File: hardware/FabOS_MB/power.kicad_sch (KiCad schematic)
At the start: 22 parts, among them U501 TDPOWER TAS12-5-W2, U502 TPS563201

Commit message: create pcb
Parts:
- JP501: footprint Jumper:SolderJumper-2_P1.3mm_Open_Pad1.0x1.5mm -> Jumper:SolderJumper-2_P1.3mm_Open_TrianglePad1.0x1.5mm
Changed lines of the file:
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@@
 			)
 		)
-		(property "Footprint" "Jumper:SolderJumper-2_P1.3mm_Open_Pad1.0x1.5mm"
+		(property "Footprint" "Jumper:SolderJumper-2_P1.3mm_Open_TrianglePad1.0x1.5mm"
 			(at 82.55 36.83 0)
 			(effects

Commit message: Placement des composants
On va mourir
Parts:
- C502, C503: footprint Capacitor_SMD:C_Elec_4x5.4 -> Capacitor_SMD:C_0402_1005Metric; LCSC C213487 -> C15525; MPN VT1C100M0405 -> CL05A106MQ5NUNC
- C505: footprint Capacitor_SMD:C_Elec_6.3x5.4 -> Capacitor_SMD:C_0201_0603Metric_Pad0.64x0.40mm_HandSolder; LCSC C72505 -> C59461; MPN RVT1H220M0605 -> CL10A226MQ8NRNC
- C506: footprint Capacitor_SMD:C_Elec_6.3x5.4 -> Capacitor_SMD:C_0201_0603Metric_Pad0.64x0.40mm_HandSolder; LCSC (none) -> C59461; MPN (none) -> CL10A226MQ8NRNC
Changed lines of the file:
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@@
 			)
 		)
-		(property "Footprint" "Capacitor_SMD:C_Elec_6.3x5.4"
+		(property "Footprint" "Capacitor_SMD:C_0201_0603Metric_Pad0.64x0.40mm_HandSolder"
 			(at 210.82 116.84 0)
 			(effects
@@
 			)
 		)
-		(property "Datasheet" "https://www.lcsc.com/product-detail/Aluminum-Electrolytic-Capacitors-SMD_ROQANG-RVT1H220M0605_C72505.html"
+		(property "Datasheet" "https://www.lcsc.com/datasheet/lcsc_datasheet_2304140030_Samsung-Electro-Mechanics-CL10A226MQ8NRNC_C59461.pdf"
 			(at 210.82 116.84 0)
 			(effects
@@
 			)
 		)
-		(property "MPN" " RVT1H220M0605"
+		(property "MPN" "CL10A226MQ8NRNC"
 			(at 210.82 116.84 0)
 			(effects
@@
 			)
 		)
-		(property "LCSC" " C72505"
+		(property "LCSC" "C59461"
 			(at 210.82 116.84 0)
 			(effects
@@
 				(path "/09377d5d-727f-4ff4-92c8-7a0483d23f1e/97fc260e-c16c-48c4-b11a-4f8ec3a451f5"
 					(reference "C505")
+					(unit 1)
+				)
+			)
+		)
+	)
+	(symbol
+		(lib_id "Device:C_Small")
+		(at 220.98 116.84 0)
+		(mirror y)
+		(unit 1)
+		(exclude_from_sim no)
+		(in_bom yes)
+		(on_board yes)
+		(dnp no)
+		(fields_autoplaced yes)
+		(property "Reference" "C506"
+			(at 218.44 115.5762 0)
+			(effects
+				(font
+					(size 1.27 1.27)
+				)
+				(justify left)
+			)
+		)
+		(property "Value" "22u"
+			(at 218.44 118.1162 0)
+			(effects
+				(font
+					(size 1.27 1.27)
+				)
+				(justify left)
+			)
+		)
+		(property "Footprint" "Capacitor_SMD:C_0201_0603Metric_Pad0.64x0.40mm_HandSolder"
+			(at 220.98 116.84 0)
+			(effects
+				(font
+					(size 1.27 1.27)
+				)
+				(hide yes)
+			)
+		)
+		(property "Datasheet" "https://www.lcsc.com/datasheet/lcsc_datasheet_2304140030_Samsung-Electro-Mechanics-CL10A226MQ8NRNC_C59461.pdf"
+			(at 220.98 116.84 0)
+			(effects
+				(font
+					(size 1.27 1.27)
+				)
+				(hide yes)
+			)
+		)
+		(property "Description" "Unpolarized capacitor, small symbol"
+			(at 220.98 116.84 0)
+			(effects
+				(font
+					(size 1.27 1.27)
+				)
+				(hide yes)
+			)
+		)
+		(property "MPN" "CL10A226MQ8NRNC"
+			(at 220.98 116.84 0)
+			(effects
+				(font
+					(size 1.27 1.27)
+				)
+				(hide yes)
+			)
+		)
+		(property "LCSC" "C59461"
+			(at 220.98 116.84 0)
+			(effects
+				(font
+					(size 1.27 1.27)
+				)
+				(hide yes)
+			)
+		)
+		(pin "1"
+		)
+		(pin "2"
+		)
+		(instances
+			(project "FabOS_MB"
+				(path "/09377d5d-727f-4ff4-92c8-7a0483d23f1e/97fc260e-c16c-48c4-b11a-4f8ec3a451f5"
+					(reference "C506")
 					(unit 1)
 				)
@@
 	(symbol
 		(lib_id "Device:C_Small")
-		(at 220.98 116.84 0)
-		(mirror y)
-		(unit 1)
-		(exclude_from_sim no)
-		(in_bom yes)
-		(on_board yes)
-		(dnp no)
-		(fields_autoplaced yes)
-		(property "Reference" "C506"
-			(at 218.44 115.5762 0)
-			(effects
-				(font
-					(size 1.27 1.27)
-				)
-				(justify left)
-			)
-		)
-		(property "Value" "22u"
-			(at 218.44 118.1162 0)
-			(effects
-				(font
-					(size 1.27 1.27)
-				)
-				(justify left)
-			)
-		)
-		(property "Footprint" "Capacitor_SMD:C_Elec_6.3x5.4"
-			(at 220.98 116.84 0)
-			(effects
-				(font
-					(size 1.27 1.27)
-				)
-				(hide yes)
-			)
-		)
-		(property "Datasheet" "~"
-			(at 220.98 116.84 0)
-			(effects
-				(font
-					(size 1.27 1.27)
-				)
-				(hide yes)
-			)
-		)
-		(property "Description" "Unpolarized capacitor, small symbol"
-			(at 220.98 116.84 0)
-			(effects
-				(font
-					(size 1.27 1.27)
-				)
-				(hide yes)
-			)
-		)
-		(pin "1"
-		)
-		(pin "2"
-		)
-		(instances
-			(project "FabOS_MB"
-				(path "/09377d5d-727f-4ff4-92c8-7a0483d23f1e/97fc260e-c16c-48c4-b11a-4f8ec3a451f5"
-					(reference "C506")
-					(unit 1)
-				)
-			)
-		)
-	)
-	(symbol
-		(lib_id "Device:C_Small")
 		(at 184.15 109.22 0)
 		(unit 1)
@@
 			)
 		)
-		(property "Footprint" "Capacitor_SMD:C_Elec_4x5.4"
+		(property "Footprint" "Capacitor_SMD:C_0402_1005Metric"
 			(at 129.54 109.22 0)
 			(effects
@@
 			)
 		)
-		(property "Datasheet" "https://www.lcsc.com/product-detail/Aluminum-Electrolytic-Capacitors-SMD_ROQANG-VT1C100M0405_C213487.html"
+		(property "Datasheet" "https://www.lcsc.com/datasheet/lcsc_datasheet_2208231630_Samsung-Electro-Mechanics-CL05A106MQ5NUNC_C15525.pdf"
 			(at 129.54 109.22 0)
 			(effects
@@
 			)
 		)
-		(property "MPN" "VT1C100M0405"
+		(property "MPN" "CL05A106MQ5NUNC"
 			(at 131.572 116.332 0)
 			(effects
@@
 			)
 		)
-		(property "LCSC" " C213487"
+		(property "LCSC" "C15525"
 			(at 129.54 109.22 0)
 			(effects
@@
 	)
 	(symbol
+		(lib_id "Device:C_Small")
+		(at 138.43 109.22 0)
+		(unit 1)
+		(exclude_from_sim no)
+		(in_bom yes)
+		(on_board yes)
+		(dnp no)
+		(property "Reference" "C503"
+			(at 132.08 110.744 0)
+			(effects
+				(font
+					(size 1.27 1.27)
+				)
+				(justify left)
+			)
+		)
+		(property "Value" "10u"
+			(at 133.35 107.95 0)
+			(effects
+				(font
+					(size 1.27 1.27)
+				)
+				(justify left)
+			)
+		)
+		(property "Footprint" "Capacitor_SMD:C_0402_1005Metric"
+			(at 138.43 109.22 0)
+			(effects
+				(font
+					(size 1.27 1.27)
+				)
+				(hide yes)
+			)
+		)
+		(property "Datasheet" "https://www.lcsc.com/datasheet/lcsc_datasheet_2208231630_Samsung-Electro-Mechanics-CL05A106MQ5NUNC_C15525.pdf"
+			(at 138.43 109.22 0)
+			(effects
+				(font
+					(size 1.27 1.27)
+				)
+				(hide yes)
+			)
+		)
+		(property "Description" "Unpolarized capacitor, small symbol"
+			(at 138.43 109.22 0)
+			(effects
+				(font
+					(size 1.27 1.27)
+				)
+				(hide yes)
+			)
+		)
+		(property "MPN" "CL05A106MQ5NUNC"
+			(at 140.462 116.332 0)
+			(effects
+				(font
+					(size 1.27 1.27)
+				)
+				(hide yes)
+			)
+		)
+		(property "LCSC" "C15525"
+			(at 138.43 109.22 0)
+			(effects
+				(font
+					(size 1.27 1.27)
+				)
+				(hide yes)
+			)
+		)
+		(pin "1"
+		)
+		(pin "2"
+		)
+		(instances
+			(project "FabOS_MB"
+				(path "/09377d5d-727f-4ff4-92c8-7a0483d23f1e/97fc260e-c16c-48c4-b11a-4f8ec3a451f5"
+					(reference "C503")
+					(unit 1)
+				)
+			)
+		)
+	)
+	(symbol
 		(lib_id "power:Earth")
 		(at 46.99 40.64 0)
@@
 					(unit 1)
 				)
-			)
-		)
-	)
-	(symbol
-		(lib_id "Device:C_Small")
-		(at 138.43 109.22 0)
-		(unit 1)
-		(exclude_from_sim no)
-		(in_bom yes)
-		(on_board yes)
-		(dnp no)
-		(property "Reference" "C503"
-			(at 131.826 107.696 0)
-			(effects
-				(font
-					(size 1.27 1.27)
-				)
-				(justify left)
-			)
-		)
-		(property "Value" "10u"
-			(at 132.842 110.744 0)
-			(effects
-				(font
-					(size 1.27 1.27)
-				)
-				(justify left)
-			)
-		)
-		(property "Footprint" "Capacitor_SMD:C_Elec_4x5.4"
-			(at 138.43 109.22 0)
-			(effects
-				(font
-					(size 1.27 1.27)
-				)
-				(hide yes)
-			)
-		)
-		(property "Datasheet" "https://www.lcsc.com/product-detail/Aluminum-Electrolytic-Capacitors-SMD_ROQANG-VT1C100M0405_C213487.html"
-			(at 138.43 109.22 0)
-			(effects
-				(font
-					(size 1.27 1.27)
-				)
-				(hide yes)
-			)
-		)
-		(property "Description" "Unpolarized capacitor, small symbol"
-			(at 138.43 109.22 0)
-			(effects
-				(font
-					(size 1.27 1.27)
-				)
-				(hide yes)
-			)
-		)
-		(property "MPN" "VT1C100M0405"
-			(at 140.462 116.332 0)
-			(effects
-				(font
-					(size 1.27 1.27)
-				)
-				(hide yes)
-			)
-		)
-		(property "LCSC" " C213487"
-			(at 138.43 109.22 0)
-			(effects
-				(font
-					(size 1.27 1.27)
-				)
-				(hide yes)
-			)
-		)
-		(pin "1"
-		)
-		(pin "2"
-		)
-		(instances
-			(project "FabOS_MB"
-				(path "/09377d5d-727f-4ff4-92c8-7a0483d23f1e/97fc260e-c16c-48c4-b11a-4f8ec3a451f5"
-					(reference "C503")
-					(unit 1)
-				)

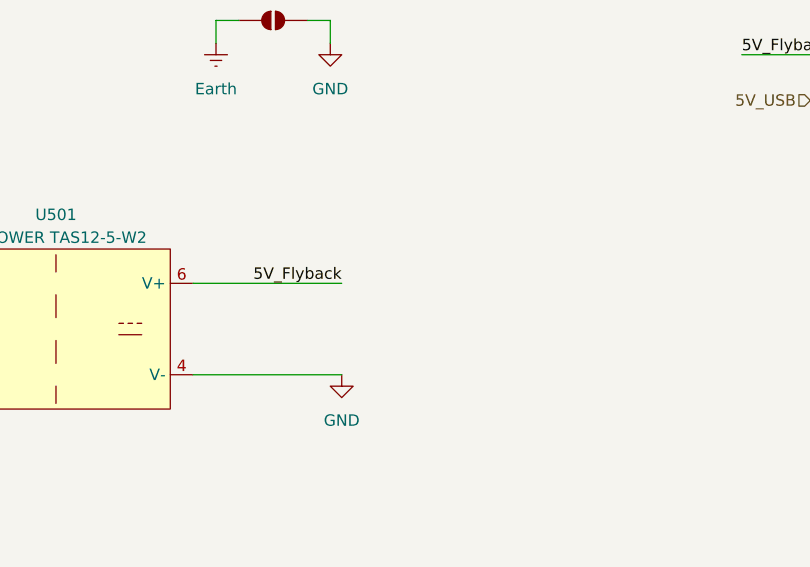
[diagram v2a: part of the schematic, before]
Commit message: update components placement
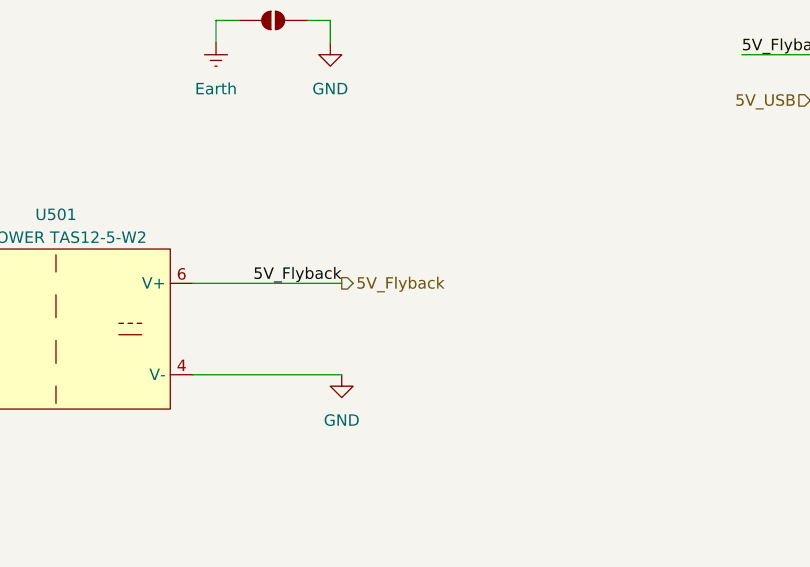
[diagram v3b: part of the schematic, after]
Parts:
- L501: footprint Inductor_SMD:L_0402_1005Metric -> Inductor_SMD:L_1206_3216Metric
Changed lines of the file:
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@@
+		)
+	)
+	(hierarchical_label "5V_Flyback"
+		(shape output)
+		(at 90.17 66.04 0)
+		(fields_autoplaced yes)
+		(effects
+			(font
+				(size 1.27 1.27)
+			)
+			(justify left)
 		)
 	)
@@
 			)
 		)
-		(property "Footprint" "Inductor_SMD:L_0402_1005Metric"
+		(property "Footprint" "Inductor_SMD:L_1206_3216Metric"
 			(at 201.93 113.03 0)
 			(effects

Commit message: update pcb routing
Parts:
- C505, C506: footprint Capacitor_SMD:C_0201_0603Metric_Pad0.64x0.40mm_HandSolder -> Capacitor_SMD:C_0603_1608Metric
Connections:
- net +3.3V: now reaches R504.1
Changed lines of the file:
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@@
 			)
 		)
-		(property "Footprint" "Capacitor_SMD:C_0201_0603Metric_Pad0.64x0.40mm_HandSolder"
+		(property "Footprint" "Capacitor_SMD:C_0603_1608Metric"
 			(at 210.82 116.84 0)
 			(effects
@@
 			)
 		)
-		(property "Footprint" "Capacitor_SMD:C_0201_0603Metric_Pad0.64x0.40mm_HandSolder"
+		(property "Footprint" "Capacitor_SMD:C_0603_1608Metric"
 			(at 220.98 116.84 0)
 			(effects
@@
 	)
 	(symbol
+		(lib_id "power:+3.3V")
+		(at 204.47 29.21 0)
+		(unit 1)
+		(exclude_from_sim no)
+		(in_bom yes)
+		(on_board yes)
+		(dnp no)
+		(fields_autoplaced yes)
+		(property "Reference" "#PWR02"
+			(at 204.47 33.02 0)
+			(effects
+				(font
+					(size 1.27 1.27)
+				)
+				(hide yes)
+			)
+		)
+		(property "Value" "+3.3V"
+			(at 204.47 24.13 0)
+			(effects
+				(font
+					(size 1.27 1.27)
+				)
+			)
+		)
+		(property "Footprint" ""
+			(at 204.47 29.21 0)
+			(effects
+				(font
+					(size 1.27 1.27)
+				)
+				(hide yes)
+			)
+		)
+		(property "Datasheet" ""
+			(at 204.47 29.21 0)
+			(effects
+				(font
+					(size 1.27 1.27)
+				)
+				(hide yes)
+			)
+		)
+		(property "Description" "Power symbol creates a global label with name \"+3.3V\""
+			(at 204.47 29.21 0)
+			(effects
+				(font
+					(size 1.27 1.27)
+				)
+				(hide yes)
+			)
+		)
+		(pin "1"
+		)
+		(instances
+			(project ""
+				(path "/09377d5d-727f-4ff4-92c8-7a0483d23f1e/97fc260e-c16c-48c4-b11a-4f8ec3a451f5"
+					(reference "#PWR02")
+					(unit 1)
+				)
+			)
+		)
+	)
+	(symbol
 		(lib_name "Conn_01x03_1")
 		(lib_id "Connector_Generic:Conn_01x03")
@@
 					(unit 1)
 				)
-			)
-		)
-	)
-	(symbol
-		(lib_id "power:+3.3V")
-		(at 204.47 29.21 0)
-		(unit 1)
-		(exclude_from_sim no)
-		(in_bom yes)
-		(on_board yes)
-		(dnp no)
-		(fields_autoplaced yes)
-		(property "Reference" "#PWR0512"
-			(at 204.47 33.02 0)
-			(effects
-				(font
-					(size 1.27 1.27)
-				)
-				(hide yes)
-			)
-		)
-		(property "Value" "+3.3V"
-			(at 204.47 24.13 0)
-			(effects
-				(font
-					(size 1.27 1.27)
-				)
-			)
-		)
-		(property "Footprint" ""
-			(at 204.47 29.21 0)
-			(effects
-				(font
-					(size 1.27 1.27)
-				)
-				(hide yes)
-			)
-		)
-		(property "Datasheet" ""
-			(at 204.47 29.21 0)
-			(effects
-				(font
-					(size 1.27 1.27)
-				)
-				(hide yes)
-			)
-		)
-		(property "Description" "Power symbol creates a global label with name \"+3.3V\""
-			(at 204.47 29.21 0)
-			(effects
-				(font
-					(size 1.27 1.27)
-				)
-				(hide yes)
-			)
-		)
-		(pin "1"
-		)
-		(instances
-			(project ""
-				(path "/09377d5d-727f-4ff4-92c8-7a0483d23f1e/97fc260e-c16c-48c4-b11a-4f8ec3a451f5"
-					(reference "#PWR0512")
-					(unit 1)
-				)

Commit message: update pcb
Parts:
- D501, D502: LCSC (none) -> C133103
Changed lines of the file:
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@@
+			)
+		)
+		(property "LCSC" "C133103"
+			(at 152.4 40.64 0)
+			(effects
+				(font
+					(size 1.27 1.27)
+				)
+				(hide yes)
 			)
 		)
@@
 			(at 152.4 45.72 0)
 			(effects
+				(font
+					(size 1.27 1.27)
+				)
+				(hide yes)
+			)
+		)
+		(property "LCSC" "C133103"
+			(at 152.4 45.72 0)
+			(effects

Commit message: MàJ BoM dans Kicad
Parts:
- C501, C504: LCSC (none) -> C361203
- D501, D502: LCSC C133103 -> C154819
- D503, D504, D505: LCSC (none) -> C397046
- L501: LCSC (none) -> C139249
- R501, R502: LCSC (none) -> C25744
- R503: LCSC (none) -> C162863
- R504: LCSC (none) -> C103166
- R505, R506: LCSC (none) -> C100323
- e501: LCSC (none) -> C8377
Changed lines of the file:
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@@
+			)
+		)
+		(property "LCSC" "C100323"
+			(at 227.33 38.1 0)
+			(effects
+				(font
+					(size 1.27 1.27)
+				)
+				(hide yes)
 			)
 		)
@@
 			)
 		)
+		(property "LCSC" "C100323"
+			(at 215.9 38.1 0)
+			(effects
+				(font
+					(size 1.27 1.27)
+				)
+				(hide yes)
+			)
+		)
 		(pin "1"
 		)
@@
 			)
 		)
+		(property "LCSC" "C397046"
+			(at 215.9 48.26 0)
+			(effects
+				(font
+					(size 1.27 1.27)
+				)
+				(hide yes)
+			)
+		)
 		(pin "2"
 		)
@@
 			)
 		)
+		(property "LCSC" "C25744"
+			(at 154.94 113.03 0)
+			(effects
+				(font
+					(size 1.27 1.27)
+				)
+				(hide yes)
+			)
+		)
 		(pin "2"
 		)
@@
 			)
 		)
+		(property "LCSC" "C139249"
+			(at 201.93 113.03 0)
+			(effects
+				(font
+					(size 1.27 1.27)
+				)
+				(hide yes)
+			)
+		)
 		(pin "1"
 		)
@@
 			)
 		)
-		(property "LCSC" "C133103"
+		(property "LCSC" "C154819"
 			(at 152.4 40.64 0)
 			(effects
@@
 			)
 		)
+		(property "LCSC" "C361203 "
+			(at 184.15 109.22 0)
+			(effects
+				(font
+					(size 1.27 1.27)
+				)
+				(hide yes)
+			)
+		)
 		(pin "1"
 		)
@@
 			)
 		)
-		(property "LCSC" "C133103"
+		(property "LCSC" "C154819"
 			(at 152.4 45.72 0)
 			(effects
@@
 			)
 		)
+		(property "LCSC" "C8377"
+			(at 41.91 38.1 0)
+			(effects
+				(font
+					(size 1.27 1.27)
+				)
+				(hide yes)
+			)
+		)
 		(pin "1"
 		)
@@
 			)
 		)
+		(property "LCSC" "C162863"
+			(at 187.96 120.65 0)
+			(effects
+				(font
+					(size 1.27 1.27)
+				)
+				(hide yes)
+			)
+		)
 		(pin "1"
 		)
@@
 			)
 		)
+		(property "LCSC" "C397046"
+			(at 204.47 48.26 0)
+			(effects
+				(font
+					(size 1.27 1.27)
+				)
+				(hide yes)
+			)
+		)
 		(pin "2"
 		)
@@
 			)
 		)
+		(property "LCSC" "C397046"
+			(at 227.33 48.26 0)
+			(effects
+				(font
+					(size 1.27 1.27)
+				)
+				(hide yes)
+			)
+		)
 		(pin "2"
 		)
@@
 			)
 		)
+		(property "LCSC" "C25744"
+			(at 182.88 125.73 0)
+			(effects
+				(font
+					(size 1.27 1.27)
+				)
+				(hide yes)
+			)
+		)
 		(pin "1"
 		)
@@
 			)
 		)
+		(property "LCSC" "C103166"
+			(at 204.47 38.1 0)
+			(effects
+				(font
+					(size 1.27 1.27)
+				)
+				(hide yes)
+			)
+		)
 		(pin "1"
 		)
@@
 			(at 120.65 109.22 0)
 			(effects
+				(font
+					(size 1.27 1.27)
+				)
+				(hide yes)
+			)
+		)
+		(property "LCSC" "C361203 "
+			(at 120.65 109.22 0)
+			(effects
